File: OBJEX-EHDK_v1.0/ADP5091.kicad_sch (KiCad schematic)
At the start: 26 parts

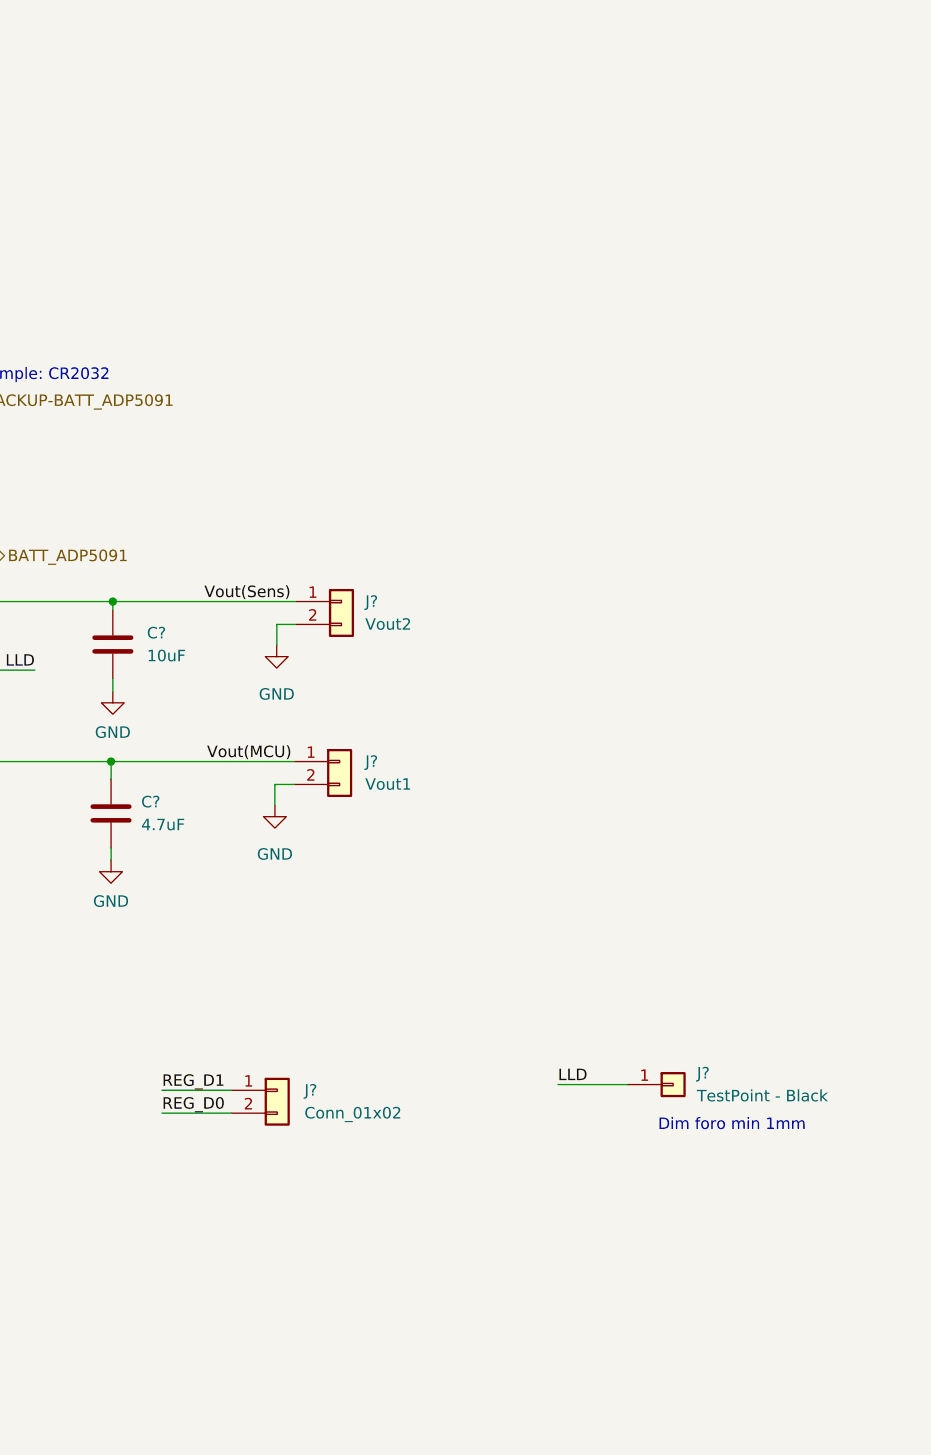
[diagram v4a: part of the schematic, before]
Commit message: Fix, add test points
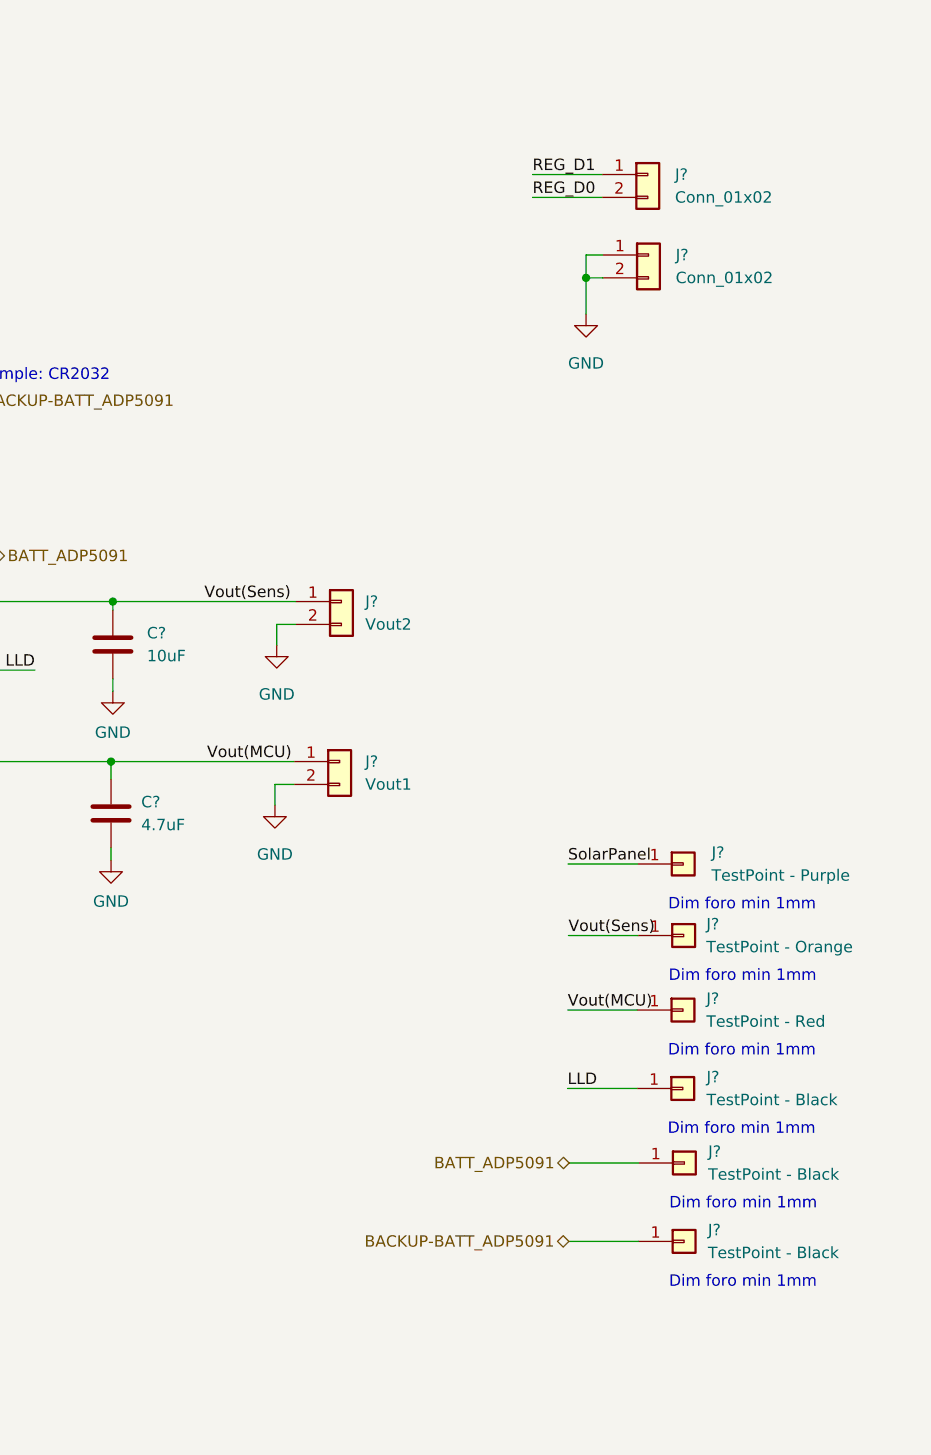
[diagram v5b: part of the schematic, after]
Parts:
- added J?: TestPoint - Orange, symbol Connector_Generic:Conn_01x01
- added J?: Conn_01x02, symbol Connector_Generic:Conn_01x02
- added J?: TestPoint - Red, symbol Connector_Generic:Conn_01x01
- added J?: TestPoint - Purple, symbol Connector_Generic:Conn_01x01
- added J? (x2): TestPoint - Black, symbol Connector_Generic:Conn_01x01
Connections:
- net BACKUP-BATT_ADP5091: now also J?.1 (Pin_1)
- net BATT_ADP5091: now also J?.1 (Pin_1)
- net GND: now also J?.1 (Pin_1), J?.2 (Pin_2)
- net SolarPanel: now also J?.1 (Pin_1)
- net Vout(MCU): now also J?.1 (Pin_1)
- net Vout(Sens): now also J?.1 (Pin_1)
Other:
- moved on the sheet: J?

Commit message: SCH Ready for first review
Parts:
- C10, C9: renamed from C?; footprint (none) -> Capacitor_SMD:C_0603_1608Metric
- C7, C8: renamed from C?; footprint (none) -> Capacitor_SMD:C_0402_1005Metric
- J15, J16, J17, J18, J19: renamed from J?; footprint (none) -> Connector_PinHeader_2.54mm:PinHeader_1x02_P2.54mm_Vertical
- J20, J21, J22, J23, J24, J25: renamed from J?; footprint (none) -> TestPoint:TestPoint_Loop_D3.80mm_Drill2.0mm
- JP1: renamed from JP?; footprint (none) -> Jumper:SolderJumper-3_P1.3mm_Open_Pad1.0x1.5mm_NumberLabels
- L2: renamed from L?; footprint (none) -> Inductor_SMD:L_0603_1608Metric
- R10, R11, R12, R13, R14, R15, R16, R17, R18, R19, R20, R7, R8, R9: renamed from R?; footprint (none) -> Resistor_SMD:R_0603_1608Metric
- gave numbers to parts that had none: 1

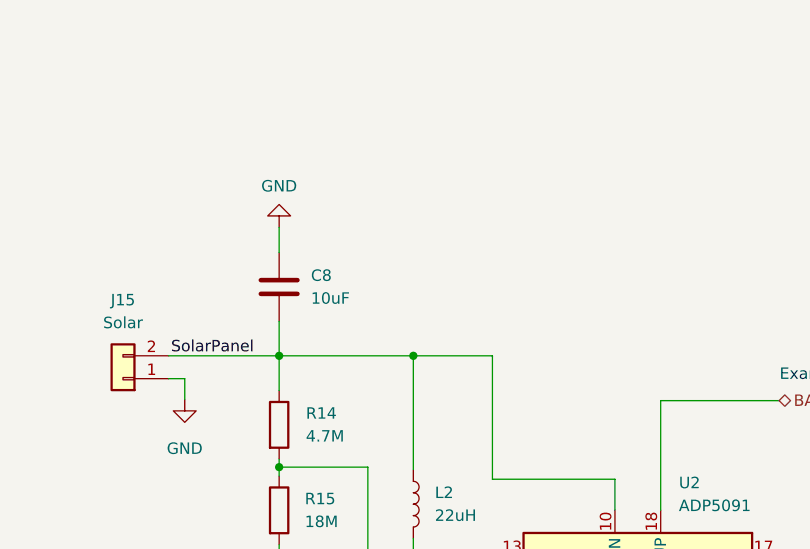
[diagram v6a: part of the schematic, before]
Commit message: SCH Ready for PCB design
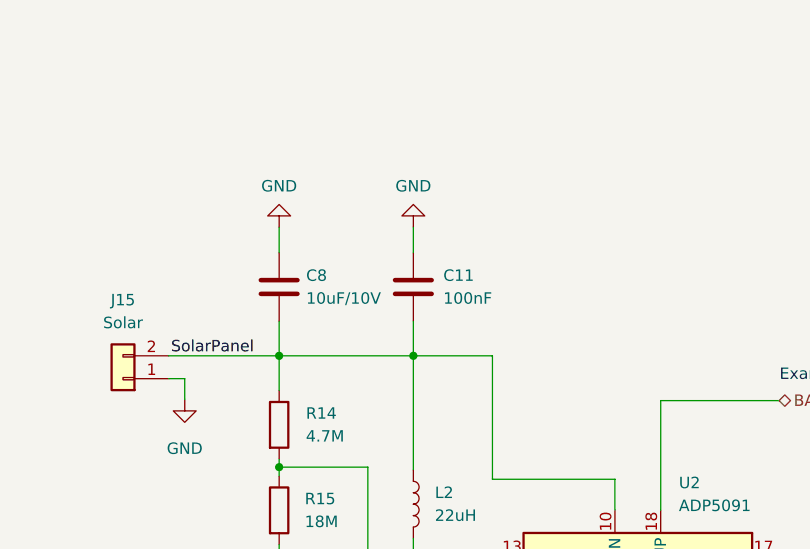
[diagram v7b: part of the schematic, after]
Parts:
- added C11: 100nF, Capacitor_SMD:C_0402_1005Metric, symbol Device:C
- C8: value 10uF -> 10uF/10V
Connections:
- net GND: now also C11.1
- net SolarPanel: now also C11.2
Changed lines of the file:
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@@
+    (stroke (width 0) (type default) (color 0 0 0 0))
+  )
+  (wire (pts (xy 137.6426 51.8922) (xy 137.6426 55.7276))
     (stroke (width 0) (type default) (color 0 0 0 0))
   )
@@
   )
   (wire (pts (xy 147.3454 116.0526) (xy 143.0528 116.0526))
+    (stroke (width 0) (type default) (color 0 0 0 0))
+  )
+  (wire (pts (xy 137.6426 44.2722) (xy 137.6426 41.4528))
     (stroke (width 0) (type default) (color 0 0 0 0))
   )
@@
     (pin "2")
   )
+  (symbol (lib_id "power:GND") (at 137.6426 41.4528 180) (unit 1)
+    (in_bom yes) (on_board yes) (fields_autoplaced)
+    (property "Reference" "#PWR0137" (id 0) (at 137.6426 35.1028 0)
+      (effects (font (size 1.27 1.27)) hide)
+    )
+    (property "Value" "GND" (id 1) (at 137.6426 36.8808 0))
+    (property "Footprint" "" (id 2) (at 137.6426 41.4528 0)
+      (effects (font (size 1.27 1.27)) hide)
+    )
+    (property "Datasheet" "" (id 3) (at 137.6426 41.4528 0)
+      (effects (font (size 1.27 1.27)) hide)
+    )
+    (pin "1")
+  )
   (symbol (lib_id "Connector_Generic:Conn_01x02") (at 219.4052 100.8126 0) (unit 1)
     (in_bom yes) (on_board yes) (fields_autoplaced)
@@
     )
     (pin "1")
+  )
+  (symbol (lib_id "Device:C") (at 137.6426 48.0822 0) (unit 1)
+    (in_bom yes) (on_board yes) (fields_autoplaced)
+    (property "Reference" "C11" (id 0) (at 140.97 46.8121 0)
+      (effects (font (size 1.27 1.27)) (justify left))
+    )
+    (property "Value" "100nF" (id 1) (at 140.97 49.3521 0)
+      (effects (font (size 1.27 1.27)) (justify left))
+    )
+    (property "Footprint" "Capacitor_SMD:C_0402_1005Metric" (id 2) (at 138.6078 51.8922 0)
+      (effects (font (size 1.27 1.27)) hide)
+    )
+    (property "Datasheet" "~" (id 3) (at 137.6426 48.0822 0)
+      (effects (font (size 1.27 1.27)) hide)
+    )
+    (pin "1")
+    (pin "2")
   )
   (symbol (lib_id "power:GND") (at 246.7864 51.1048 0) (unit 1)
@@
   (symbol (lib_id "Device:C") (at 122.7328 48.0822 0) (unit 1)
     (in_bom yes) (on_board yes) (fields_autoplaced)
-    (property "Reference" "C8" (id 0) (at 126.2634 46.8121 0)
-      (effects (font (size 1.27 1.27)) (justify left))
-    )
-    (property "Value" "10uF" (id 1) (at 126.2634 49.3521 0)
-      (effects (font (size 1.27 1.27)) (justify left))
-    )
+    (property "Reference" "C8" (id 0) (at 125.73 46.8121 0)
+      (effects (font (size 1.27 1.27)) (justify left))
+    )
+    (property "Value" "10uF/10V" (id 1) (at 125.73 49.3521 0)
+      (effects (font (size 1.27 1.27)) (justify left))
+    )

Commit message: SCH first review
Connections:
- net at U2.20 (VID): now also JP1.2 (C); no longer JP1.3 (B)
- net at R8.1: now also JP1.1 (A); no longer JP1.2 (C)
- net at R7.1: now also JP1.3 (B); no longer JP1.1 (A)
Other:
- moved on the sheet: JP1, R7, R8
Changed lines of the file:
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@@
+    (stroke (width 0) (type default) (color 0 0 0 0))
+  )
+  (wire (pts (xy 69.0626 85.2678) (xy 69.0626 88.1126))
     (stroke (width 0) (type default) (color 0 0 0 0))
   )
@@
     (stroke (width 0) (type default) (color 0 0 0 0))
   )
+  (wire (pts (xy 58.547 85.2678) (xy 69.0626 85.2678))
+    (stroke (width 0) (type default) (color 0 0 0 0))
+  )
   (wire (pts (xy 137.6426 76.0222) (xy 137.6426 77.9526))
     (stroke (width 0) (type default) (color 0 0 0 0))
@@
     (stroke (width 0) (type default) (color 0 0 0 0))
   )
-  (wire (pts (xy 54.2544 93.1926) (xy 54.2544 114.5032))
+  (wire (pts (xy 58.547 85.2678) (xy 58.547 115.7986))
     (stroke (width 0) (type default) (color 0 0 0 0))
   )
@@
     (stroke (width 0) (type default) (color 0 0 0 0))
   )
-  (wire (pts (xy 67.7926 114.5286) (xy 67.7926 97.0026))
+  (wire (pts (xy 69.0626 115.7986) (xy 69.0626 98.2726))
     (stroke (width 0) (type default) (color 0 0 0 0))
   )
@@
     (stroke (width 0) (type default) (color 0 0 0 0))
   )
-  (wire (pts (xy 62.7126 93.1926) (xy 54.2544 93.1926))
-    (stroke (width 0) (type default) (color 0 0 0 0))
-  )
   (wire (pts (xy 212.217 103.3526) (xy 212.217 105.664))
     (stroke (width 0) (type default) (color 0 0 0 0))
@@
     (stroke (width 0) (type default) (color 0 0 0 0))
   )
-  (wire (pts (xy 54.2544 122.1232) (xy 54.2544 124.9426))
+  (wire (pts (xy 58.547 123.4186) (xy 58.547 126.238))
     (stroke (width 0) (type default) (color 0 0 0 0))
   )
@@
     (stroke (width 0) (type default) (color 0 0 0 0))
   )
-  (wire (pts (xy 67.7926 122.1486) (xy 67.7926 124.968))
+  (wire (pts (xy 69.0626 123.4186) (xy 69.0626 126.238))
     (stroke (width 0) (type default) (color 0 0 0 0))
   )
@@
     (effects (font (size 5 5) (thickness 0.8) bold) (justify left bottom))
   )
-  (text "55.6K = Vout 3.3V" (at 66.4464 120.9548 90)
+  (text "55.6K = Vout 3.3V" (at 67.7164 122.2248 90)
     (effects (font (size 1.27 1.27)) (justify left bottom))
   )
@@
     (effects (font (size 3.5 3.5) italic) (justify left bottom))
   )
-  (text "14K = Vout 1.8V" (at 52.9082 120.9294 90)
+  (text "14K = Vout 1.8V" (at 57.2008 122.2248 90)
     (effects (font (size 1.27 1.27)) (justify left bottom))
   )
@@
     (pin "2")
   )
-  (symbol (lib_id "power:GND") (at 54.2544 124.9426 0) (unit 1)
-    (in_bom yes) (on_board yes) (fields_autoplaced)
-    (property "Reference" "#PWR0125" (id 0) (at 54.2544 131.2926 0)
-      (effects (font (size 1.27 1.27)) hide)
-    )
-    (property "Value" "GND" (id 1) (at 54.2544 129.5146 0))
-    (property "Footprint" "" (id 2) (at 54.2544 124.9426 0)
-      (effects (font (size 1.27 1.27)) hide)
-    )
-    (property "Datasheet" "" (id 3) (at 54.2544 124.9426 0)
+  (symbol (lib_id "power:GND") (at 58.547 126.238 0) (unit 1)
+    (in_bom yes) (on_board yes) (fields_autoplaced)
+    (property "Reference" "#PWR0125" (id 0) (at 58.547 132.588 0)
+      (effects (font (size 1.27 1.27)) hide)
+    )
+    (property "Value" "GND" (id 1) (at 58.547 130.81 0))
+    (property "Footprint" "" (id 2) (at 58.547 126.238 0)
+      (effects (font (size 1.27 1.27)) hide)
+    )
+    (property "Datasheet" "" (id 3) (at 58.547 126.238 0)
       (effects (font (size 1.27 1.27)) hide)
     )
@@
     (pin "2")
   )
-  (symbol (lib_id "power:GND") (at 67.7926 124.968 0) (unit 1)
-    (in_bom yes) (on_board yes) (fields_autoplaced)
-    (property "Reference" "#PWR0124" (id 0) (at 67.7926 131.318 0)
-      (effects (font (size 1.27 1.27)) hide)
-    )
-    (property "Value" "GND" (id 1) (at 67.7926 129.54 0))
-    (property "Footprint" "" (id 2) (at 67.7926 124.968 0)
-      (effects (font (size 1.27 1.27)) hide)
-    )
-    (property "Datasheet" "" (id 3) (at 67.7926 124.968 0)
+  (symbol (lib_id "power:GND") (at 69.0626 126.238 0) (unit 1)
+    (in_bom yes) (on_board yes) (fields_autoplaced)
+    (property "Reference" "#PWR0124" (id 0) (at 69.0626 132.588 0)
+      (effects (font (size 1.27 1.27)) hide)
+    )
+    (property "Value" "GND" (id 1) (at 69.0626 130.81 0))
+    (property "Footprint" "" (id 2) (at 69.0626 126.238 0)
+      (effects (font (size 1.27 1.27)) hide)
+    )
+    (property "Datasheet" "" (id 3) (at 69.0626 126.238 0)
       (effects (font (size 1.27 1.27)) hide)
     )
@@
     (pin "1")
   )
-  (symbol (lib_id "Device:R") (at 67.7926 118.3386 0) (unit 1)
-    (in_bom yes) (on_board yes) (fields_autoplaced)
-    (property "Reference" "R8" (id 0) (at 69.977 117.0685 0)
-      (effects (font (size 1.27 1.27)) (justify left))
-    )
-    (property "Value" "55.6K" (id 1) (at 69.977 119.6085 0)
-      (effects (font (size 1.27 1.27)) (justify left))
-    )
-    (property "Footprint" "Resistor_SMD:R_0603_1608Metric" (id 2) (at 66.0146 118.3386 90)
-      (effects (font (size 1.27 1.27)) hide)
-    )
-    (property "Datasheet" "~" (id 3) (at 67.7926 118.3386 0)
+  (symbol (lib_id "Device:R") (at 69.0626 119.6086 0) (unit 1)
+    (in_bom yes) (on_board yes) (fields_autoplaced)
+    (property "Reference" "R8" (id 0) (at 71.247 118.3385 0)
+      (effects (font (size 1.27 1.27)) (justify left))
+    )
+    (property "Value" "55.6K" (id 1) (at 71.247 120.8785 0)
+      (effects (font (size 1.27 1.27)) (justify left))
+    )
+    (property "Footprint" "Resistor_SMD:R_0603_1608Metric" (id 2) (at 67.2846 119.6086 90)
+      (effects (font (size 1.27 1.27)) hide)
+    )
+    (property "Datasheet" "~" (id 3) (at 69.0626 119.6086 0)
       (effects (font (size 1.27 1.27)) hide)
     )
@@
     (pin "2")
   )
-  (symbol (lib_id "Jumper:SolderJumper_3_Open") (at 67.7926 93.1926 0) (unit 1)
-    (in_bom yes) (on_board yes) (fields_autoplaced)
-    (property "Reference" "JP1" (id 0) (at 67.7926 86.4616 0))
-    (property "Value" "SolderJumper_3_Open" (id 1) (at 67.7926 89.0016 0))
-    (property "Footprint" "Jumper:SolderJumper-3_P1.3mm_Open_Pad1.0x1.5mm_NumberLabels" (id 2) (at 67.7926 93.1926 0)
-      (effects (font (size 1.27 1.27)) hide)
-    )
-    (property "Datasheet" "~" (id 3) (at 67.7926 93.1926 0)
+  (symbol (lib_id "Jumper:SolderJumper_3_Open") (at 69.0626 93.1926 90) (unit 1)
+    (in_bom yes) (on_board yes) (fields_autoplaced)
+    (property "Reference" "JP1" (id 0) (at 67.31 91.9225 90)
+      (effects (font (size 1.27 1.27)) (justify left))
+    )
+    (property "Value" "SolderJumper_3_Open" (id 1) (at 67.31 94.4625 90)
+      (effects (font (size 1.27 1.27)) (justify left))
+    )
+    (property "Footprint" "Jumper:SolderJumper-3_P1.3mm_Open_Pad1.0x1.5mm_NumberLabels" (id 2) (at 69.0626 93.1926 0)
+      (effects (font (size 1.27 1.27)) hide)
+    )
+    (property "Datasheet" "~" (id 3) (at 69.0626 93.1926 0)
       (effects (font (size 1.27 1.27)) hide)
     )
@@
     (pin "2")
   )
-  (symbol (lib_id "Device:R") (at 54.2544 118.3132 0) (unit 1)
-    (in_bom yes) (on_board yes) (fields_autoplaced)
-    (property "Reference" "R7" (id 0) (at 56.2864 117.0431 0)
-      (effects (font (size 1.27 1.27)) (justify left))
-    )
-    (property "Value" "14K" (id 1) (at 56.2864 119.5831 0)
-      (effects (font (size 1.27 1.27)) (justify left))
-    )
-    (property "Footprint" "Resistor_SMD:R_0603_1608Metric" (id 2) (at 52.4764 118.3132 90)
-      (effects (font (size 1.27 1.27)) hide)
-    )
-    (property "Datasheet" "~" (id 3) (at 54.2544 118.3132 0)
-      (effects (font (size 1.27 1.27)) hide)
-    )
+  (symbol (lib_id "Device:R") (at 58.547 119.6086 0) (unit 1)
+    (in_bom yes) (on_board yes) (fields_autoplaced)
+    (property "Reference" "R7" (id 0) (at 60.579 118.3385 0)
+      (effects (font (size 1.27 1.27)) (justify left))
+    )
+    (property "Value" "14K" (id 1) (at 60.579 120.8785 0)
+      (effects (font (size 1.27 1.27)) (justify left))
+    )
+    (property "Footprint" "Resistor_SMD:R_0603_1608Metric" (id 2) (at 56.769 119.6086 90)
+      (effects (font (size 1.27 1.27)) hide)
+    )
+    (property "Datasheet" "~" (id 3) (at 58.547 119.6086 0)
+      (effects (font (size 1.27 1.27)) hide)
+    )
